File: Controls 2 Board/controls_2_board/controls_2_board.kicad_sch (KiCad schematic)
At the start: 15 parts, among them J1 Conn_01x05_Socket, J2 Conn_01x04_Socket, J3 Conn_01x02_Socket, U1 UA741CDR, U2 MCP47CVB22-E/UN

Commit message: Just looking
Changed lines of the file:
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@@
-	)
-	(junction
-		(at 110.49 106.68)
-		(diameter 0)
-		(color 0 0 0 0)
 	)
 	(junction
@@
 	(junction
 		(at 209.55 109.22)
+		(diameter 0)
+		(color 0 0 0 0)
+	)
+	(junction
+		(at 107.95 100.33)
 		(diameter 0)
 		(color 0 0 0 0)
@@
 	(wire
 		(pts
-			(xy 110.49 53.34) (xy 132.08 53.34)
+			(xy 107.95 53.34) (xy 132.08 53.34)
 		)
 		(stroke
@@
 	(wire
 		(pts
-			(xy 110.49 106.68) (xy 115.57 106.68)
-		)
-		(stroke
-			(width 0)
-			(type default)
-		)
-	)
-	(wire
-		(pts
 			(xy 248.92 53.34) (xy 248.92 71.12)
 		)
@@
 	(wire
 		(pts
-			(xy 107.95 106.68) (xy 110.49 106.68)
+			(xy 107.95 106.68) (xy 115.57 106.68)
 		)
 		(stroke
@@
 	(wire
 		(pts
-			(xy 110.49 53.34) (xy 110.49 106.68)
+			(xy 107.95 53.34) (xy 107.95 100.33)
 		)
 		(stroke
@@
 	(label "SDA"
 		(at 52.07 113.03 0)
-		(fields_autoplaced yes)
 		(effects
 			(font
@@
 	(label "~{LAT}"
 		(at 36.83 68.58 0)
-		(fields_autoplaced yes)
 		(effects
 			(font
@@
 	(label "SDA"
 		(at 36.83 71.12 0)
-		(fields_autoplaced yes)
 		(effects
 			(font
@@
 	(label "~{LAT}"
 		(at 55.88 123.19 0)
-		(fields_autoplaced yes)
 		(effects
 			(font
@@
 	(label "V1"
 		(at 74.93 100.33 0)
-		(fields_autoplaced yes)
 		(effects
 			(font
@@
 	(label "V1"
 		(at 15.24 120.65 0)
-		(fields_autoplaced yes)
 		(effects
 			(font
@@
 	(label "SCL"
 		(at 36.83 73.66 0)
-		(fields_autoplaced yes)
 		(effects
 			(font
@@
 	(label "V2"
 		(at 15.24 123.19 0)
-		(fields_autoplaced yes)
 		(effects
 			(font
@@
 	(label "SCL"
 		(at 52.07 115.57 0)
-		(fields_autoplaced yes)
 		(effects
 			(font
@@
 	(label "V2"
 		(at 74.93 109.22 0)
-		(fields_autoplaced yes)
-		(effects
-			(font
+		(effects
+			(font

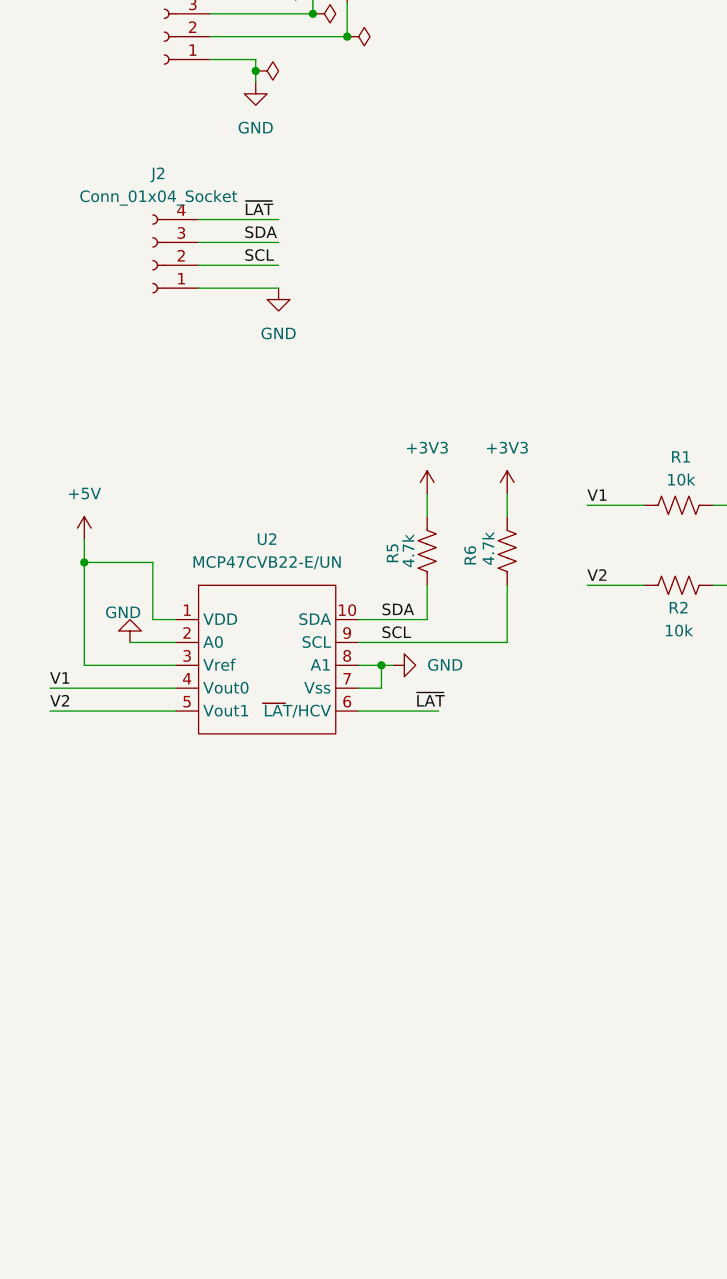
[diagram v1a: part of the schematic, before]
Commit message: Added pico
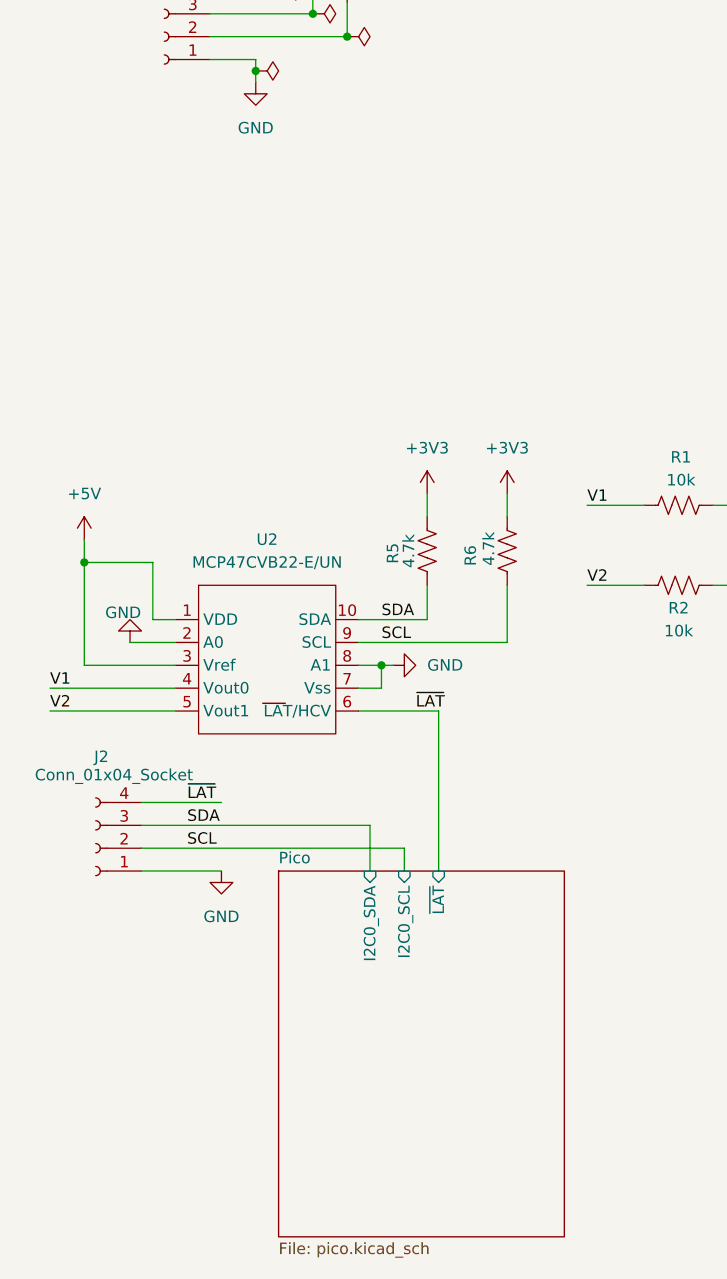
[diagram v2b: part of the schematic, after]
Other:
- added sheet Pico (pico.kicad_sch)
- moved on the sheet: J2
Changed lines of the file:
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@@
 	(wire
 		(pts
-			(xy 31.75 73.66) (xy 40.64 73.66)
+			(xy 25.4 138.43) (xy 54.61 138.43)
 		)
 		(stroke
@@
 	(wire
 		(pts
-			(xy 31.75 71.12) (xy 40.64 71.12)
+			(xy 25.4 135.89) (xy 50.8 135.89)
 		)
 		(stroke
@@
 	(wire
 		(pts
+			(xy 50.8 135.89) (xy 50.8 140.97)
+		)
+		(stroke
+			(width 0)
+			(type default)
+		)
+	)
+	(wire
+		(pts
 			(xy 248.92 53.34) (xy 248.92 71.12)
 		)
@@
 	(wire
 		(pts
+			(xy 58.42 123.19) (xy 58.42 140.97)
+		)
+		(stroke
+			(width 0)
+			(type default)
+		)
+	)
+	(wire
+		(pts
 			(xy 74.93 109.22) (xy 81.28 109.22)
 		)
@@
 	(wire
 		(pts
-			(xy 31.75 76.2) (xy 40.64 76.2)
+			(xy 25.4 140.97) (xy 34.29 140.97)
 		)
 		(stroke
@@
 	(wire
 		(pts
+			(xy 54.61 138.43) (xy 54.61 140.97)
+		)
+		(stroke
+			(width 0)
+			(type default)
+		)
+	)
+	(wire
+		(pts
 			(xy 66.04 115.57) (xy 66.04 109.22)
 		)
@@
 	(wire
 		(pts
-			(xy 31.75 68.58) (xy 40.64 68.58)
+			(xy 25.4 133.35) (xy 34.29 133.35)
 		)
 		(stroke
@@
 	)
 	(label "~{LAT}"
-		(at 36.83 68.58 0)
+		(at 30.48 133.35 0)
 		(effects
 			(font
@@
 	)
 	(label "SDA"
-		(at 36.83 71.12 0)
+		(at 30.48 135.89 0)
 		(effects
 			(font
@@
 	)
 	(label "SCL"
-		(at 36.83 73.66 0)
+		(at 30.48 138.43 0)
 		(effects
 			(font
@@
 	(symbol
 		(lib_id "power:GND")
-		(at 40.64 76.2 0)
+		(at 34.29 140.97 0)
 		(unit 1)
 		(exclude_from_sim no)
@@
 		(fields_autoplaced yes)
 		(property "Reference" "#PWR018"
-			(at 40.64 82.55 0)
+			(at 34.29 147.32 0)
 			(effects
 				(font
@@
 		)
 		(property "Value" "GND"
-			(at 40.64 81.28 0)
+			(at 34.29 146.05 0)
 			(effects
 				(font
@@
 		)
 		(property "Footprint" ""
-			(at 40.64 76.2 0)
+			(at 34.29 140.97 0)
 			(effects
 				(font
@@
 		)
 		(property "Datasheet" ""
-			(at 40.64 76.2 0)
+			(at 34.29 140.97 0)
 			(effects
 				(font
@@
 		)
 		(property "Description" "Power symbol creates a global label with name \"GND\" , ground"
-			(at 40.64 76.2 0)
+			(at 34.29 140.97 0)
 			(effects
 				(font
@@
 	(symbol
 		(lib_id "Connector:Conn_01x04_Socket")
-		(at 26.67 73.66 180)
+		(at 20.32 138.43 180)
 		(unit 1)
 		(exclude_from_sim no)
@@
 		(on_board yes)
 		(dnp no)
-		(fields_autoplaced yes)
 		(property "Reference" "J2"
-			(at 27.305 63.5 0)
+			(at 20.955 128.27 0)
 			(effects
 				(font
@@
 		)
 		(property "Value" "Conn_01x04_Socket"
-			(at 27.305 66.04 0)
+			(at 22.352 130.302 0)
 			(effects
 				(font
@@
 		)
 		(property "Footprint" "Connector_PinSocket_2.54mm:PinSocket_1x04_P2.54mm_Vertical"
-			(at 26.67 73.66 0)
+			(at 20.32 138.43 0)
 			(effects
 				(font
@@
 		)
 		(property "Datasheet" "~"
-			(at 26.67 73.66 0)
+			(at 20.32 138.43 0)
 			(effects
 				(font
@@
 		)
 		(property "Description" "Generic connector, single row, 01x04, script generated"
-			(at 26.67 73.66 0)
+			(at 20.32 138.43 0)
 			(effects
 				(font
@@
 				)
 			)
+		)
+	)
+	(sheet
+		(at 40.64 140.97)
+		(size 31.75 40.64)
+		(fields_autoplaced yes)
+		(stroke
+			(width 0.1524)
+			(type solid)
+		)
+		(fill
+			(color 0 0 0 0.0000)
+		)
+		(property "Sheetname" "Pico"
+			(at 40.64 140.2584 0)
+			(effects
+				(font
+					(size 1.27 1.27)
+				)
+				(justify left bottom)
+			)
+		)
+		(property "Sheetfile" "pico.kicad_sch"
+			(at 40.64 182.1946 0)
+			(effects
+				(font
+					(size 1.27 1.27)
+				)
+				(justify left top)
+			)
+		)
+		(pin "I2C0_SDA" input
+			(at 50.8 140.97 90)
+			(effects
+				(font
+					(size 1.27 1.27)
+				)
+				(justify right)
+			)
+		)
+		(pin "I2C0_SCL" input
+			(at 54.61 140.97 90)
+			(effects
+				(font
+					(size 1.27 1.27)
+				)
+				(justify right)
+			)
+		)
+		(pin "~{LAT}" input
+			(at 58.42 140.97 90)
+			(effects
+				(font
+					(size 1.27 1.27)
+				)
+				(justify right)
+			)
+		)
+		(instances
+			(project "controls_2_board"
+				(path "/34b50189-37ca-4c86-b9ce-0a27b911ed8e"
+					(page "2")
+				)
+			)
